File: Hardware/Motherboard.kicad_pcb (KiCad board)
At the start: 2 copper layers, 130 x 80 mm, 54 parts, among them J1 BME680, J2 JTAG, J3 Display_1, J4 Display_2, J5 Buttons, J6 USB, J7 MUSBD111M0_Supply, Q1 DMG3414U, SW1 Button_Plus, SW2 Button_Minus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

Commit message: [Hardware] Filled some empty bottom layer areas with ground plane.
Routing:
- net GND: vias 81 -> 94
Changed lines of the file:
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@@
     (thickness 1.6)
     (drawings 8)
-    (tracks 464)
+    (tracks 477)
     (zones 0)
     (modules 54)
@@
   (via (at 218.95 127.62) (size 0.8) (drill 0.4) (layers F.Cu B.Cu) (net 2))
   (via (at 218.95 130.62) (size 0.8) (drill 0.4) (layers F.Cu B.Cu) (net 2))
+  (via (at 150.162 73.66) (size 0.8) (drill 0.4) (layers F.Cu B.Cu) (net 2))
+  (via (at 150.162 76.708) (size 0.8) (drill 0.4) (layers F.Cu B.Cu) (net 2))
+  (via (at 168.958 111.76) (size 0.8) (drill 0.4) (layers F.Cu B.Cu) (net 2))
+  (via (at 177.086 119.38) (size 0.8) (drill 0.4) (layers F.Cu B.Cu) (net 2))
+  (via (at 180.388 121.412) (size 0.8) (drill 0.4) (layers F.Cu B.Cu) (net 2))
+  (via (at 182.928 121.412) (size 0.8) (drill 0.4) (layers F.Cu B.Cu) (net 2))
+  (via (at 185.468 121.412) (size 0.8) (drill 0.4) (layers F.Cu B.Cu) (net 2))
+  (via (at 188.008 121.412) (size 0.8) (drill 0.4) (layers F.Cu B.Cu) (net 2))
+  (via (at 190.548 121.412) (size 0.8) (drill 0.4) (layers F.Cu B.Cu) (net 2))
+  (via (at 193.088 121.412) (size 0.8) (drill 0.4) (layers F.Cu B.Cu) (net 2))
+  (via (at 195.628 121.666) (size 0.8) (drill 0.4) (layers F.Cu B.Cu) (net 2))
+  (via (at 170.482 87.63) (size 0.8) (drill 0.4) (layers F.Cu B.Cu) (net 2))
+  (via (at 174.038 87.63) (size 0.8) (drill 0.4) (layers F.Cu B.Cu) (net 2))
   (segment (start 168.91 83.82) (end 168.91 93.075) (width 0.5) (layer F.Cu) (net 3))
   (segment (start 171.26 95.425) (end 171.26 95.9) (width 0.5) (layer F.Cu) (net 3))

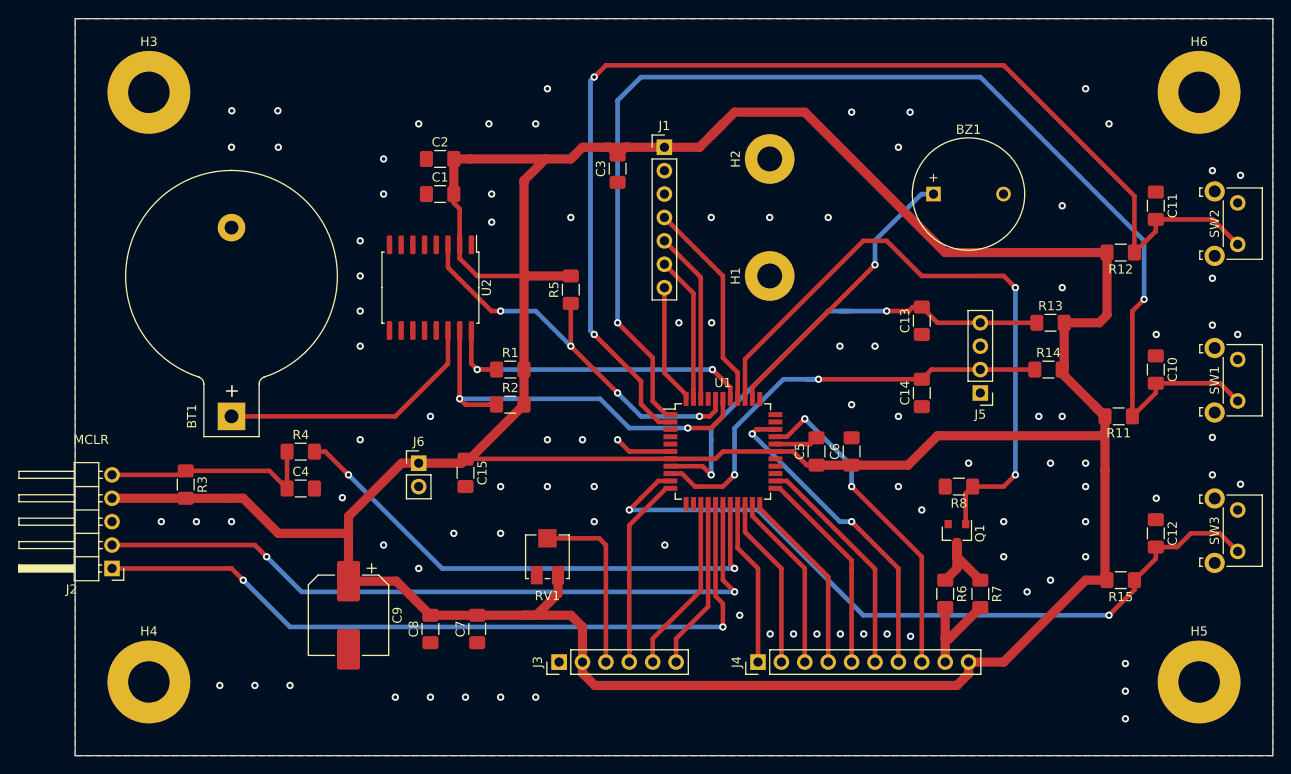
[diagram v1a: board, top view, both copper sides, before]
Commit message: [Hardware] Displayed connectors usage and button names on PCB.
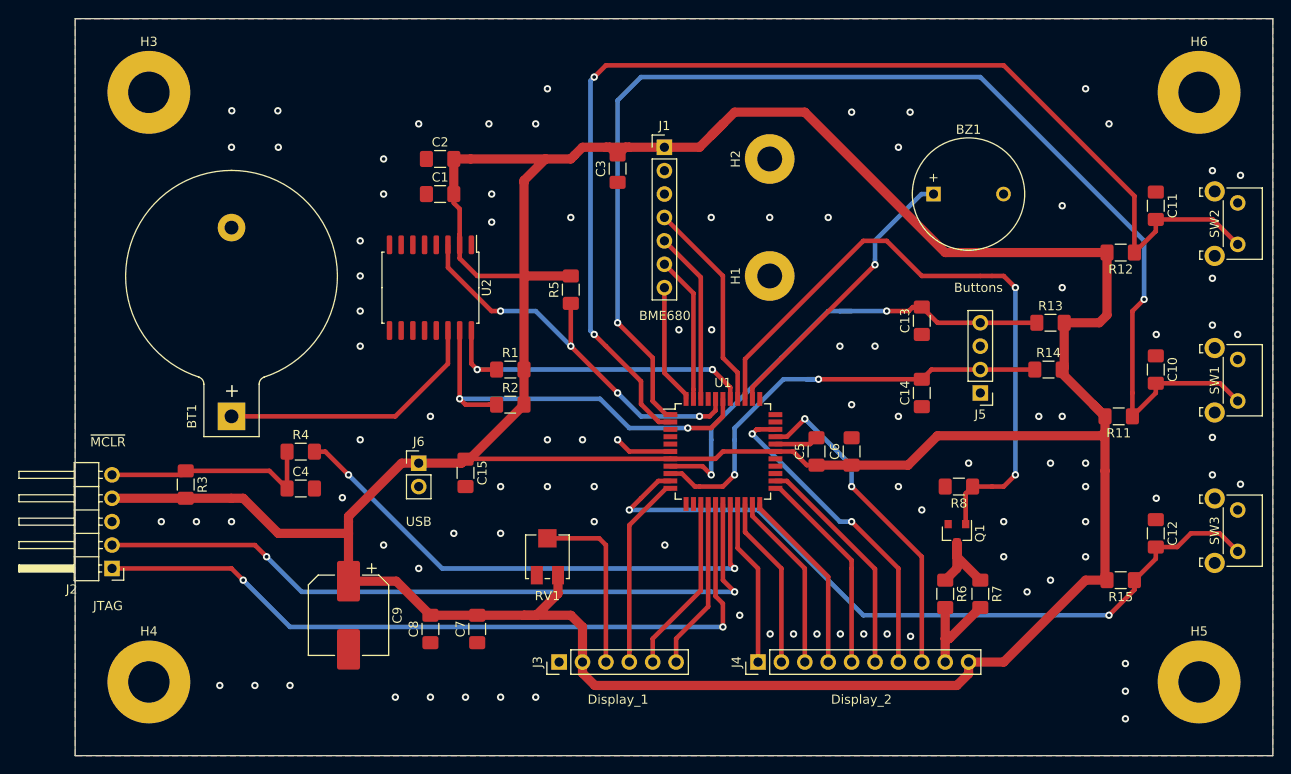
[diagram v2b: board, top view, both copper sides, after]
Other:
- board text added: "+"
- board text added: "-"
- board text added: "SET"
- board text added: "~MCLR~"
- board text removed: "MCLR"
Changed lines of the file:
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@@
   (general
     (thickness 1.6)
-    (drawings 8)
+    (drawings 11)
     (tracks 477)
     (zones 0)
@@
   )
   (setup
-    (last_trace_width 1)
+    (last_trace_width 0.5)
     (user_trace_width 0.5)
     (user_trace_width 1)
@@
       (effects (font (size 1 1) (thickness 0.15)))
     )
-    (fp_text value USB (at 0 4.87) (layer F.Fab)
+    (fp_text value USB (at 0 6.35) (layer F.SilkS)
       (effects (font (size 1 1) (thickness 0.15)))
     )
@@
       (effects (font (size 1 1) (thickness 0.15)))
     )
-    (fp_text value Buttons (at 0 9.95) (layer F.Fab)
+    (fp_text value Buttons (at 0.206 11.43) (layer F.SilkS)
       (effects (font (size 1 1) (thickness 0.15)))
     )
@@
       (effects (font (size 1 1) (thickness 0.15)))
     )
-    (fp_text value Display_2 (at 0 25.19 90) (layer F.Fab)
+    (fp_text value Display_2 (at -4.064 11.224 180) (layer F.SilkS)
       (effects (font (size 1 1) (thickness 0.15)))
     )
@@
       (effects (font (size 1 1) (thickness 0.15)))
     )
-    (fp_text value Display_1 (at 0 15.03 90) (layer F.Fab)
+    (fp_text value Display_1 (at -4.064 6.398 180) (layer F.SilkS)
       (effects (font (size 1 1) (thickness 0.15)))
     )
@@
       (effects (font (size 1 1) (thickness 0.15)))
     )
-    (fp_text value JTAG (at 4.385 12.43) (layer F.Fab)
+    (fp_text value JTAG (at 0.444 -4.064) (layer F.SilkS)
       (effects (font (size 1 1) (thickness 0.15)))
     )
@@
       (effects (font (size 1 1) (thickness 0.15)))
     )
-    (fp_text value BME680 (at 0 17.57) (layer F.Fab)
+    (fp_text value BME680 (at 0.048 18.288) (layer F.SilkS)
       (effects (font (size 1 1) (thickness 0.15)))
     )
@@
     )
   )
+  (gr_text SET (at 231.442 117.348) (layer F.Mask)
+    (effects (font (size 1.5 1.5) (thickness 0.3)))
+  )
+  (gr_text - (at 231.442 100.584) (layer F.Mask)
+    (effects (font (size 1.5 1.5) (thickness 0.3)))
+  )
+  (gr_text + (at 231.442 83.82) (layer F.Mask)
+    (effects (font (size 1.5 1.5) (thickness 0.3)))
+  )
   (dimension 80 (width 0.12) (layer F.SilkS)
     (gr_text "80,000 mm" (at 91.68 94.62 90) (layer F.SilkS)
@@
     (effects (font (size 1.5 1.5) (thickness 0.3)))
   )
-  (gr_text MCLR (at 106.68 100.33) (layer F.SilkS)
+  (gr_text ~MCLR~ (at 108.506 100.584) (layer F.SilkS)
     (effects (font (size 1 1) (thickness 0.15)))
   )
@@
   (via (at 193.088 121.412) (size 0.8) (drill 0.4) (layers F.Cu B.Cu) (net 2))
   (via (at 195.628 121.666) (size 0.8) (drill 0.4) (layers F.Cu B.Cu) (net 2))
-  (via (at 170.482 87.63) (size 0.8) (drill 0.4) (layers F.Cu B.Cu) (net 2))
-  (via (at 174.038 87.63) (size 0.8) (drill 0.4) (layers F.Cu B.Cu) (net 2))
+  (via (at 170.482 88.392) (size 0.8) (drill 0.4) (layers F.Cu B.Cu) (net 2))
+  (via (at 174.038 88.392) (size 0.8) (drill 0.4) (layers F.Cu B.Cu) (net 2))
   (segment (start 168.91 83.82) (end 168.91 93.075) (width 0.5) (layer F.Cu) (net 3))
   (segment (start 171.26 95.425) (end 171.26 95.9) (width 0.5) (layer F.Cu) (net 3))

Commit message: [Hardware] Replaced each supply part by a generic one to avoid creating a new symbol for every supply part.
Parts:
- J7: value MUSBD111M0_Supply -> USB_Connector_690-W05-260-044; footprint Empty_Footprint:Empty_Footprint -> Supply:Supply_Part
- SW4, SW5, U3: footprint Empty_Footprint:Empty_Footprint -> Supply:Supply_Part
- U4: value DEM20485SYH-LY_Supply -> LCD_DEM20485SYH-LY; footprint Empty_Footprint:Empty_Footprint -> Supply:Supply_Part
- moved SW5 44.5 mm to (71.9, 66.0)
- moved J7 37.9 mm to (59.2, 92.7)
- moved SW4 29.9 mm to (59.2, 65.9)
- moved U3 22.1 mm to (59.2, 74.9)
- moved U4 15.9 mm to (59.2, 83.8)
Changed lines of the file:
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@@
     (add_net "Net-(J4-Pad9)")
+  )
+  (module Supply:Supply_Part (layer F.Cu)
+    (at 59.23 83.82)
+    (attr virtual)
+    (fp_text reference U4 (at -3.175 3.81) (layer Eco1.User)
+      (effects (font (size 1 1) (thickness 0.15)))
+    )
+    (fp_text value LCD_DEM20485SYH-LY (at 0 -0.5) (layer F.Fab) hide
+      (effects (font (size 1 1) (thickness 0.15)))
+    )
+    (fp_line (start -5.08 2.54) (end -5.08 0) (layer Eco1.User) (width 0.12))
+    (fp_line (start 5.08 2.54) (end -5.08 2.54) (layer Eco1.User) (width 0.12))
+    (fp_line (start 5.08 -2.54) (end 5.08 2.54) (layer Eco1.User) (width 0.12))
+    (fp_line (start -5.08 -2.54) (end 5.08 -2.54) (layer Eco1.User) (width 0.12))
+    (fp_line (start -5.08 0) (end -5.08 -2.54) (layer Eco1.User) (width 0.12))
+  )
+  (module Supply:Supply_Part (layer F.Cu)
+    (at 59.23 74.93)
+    (attr virtual)
+    (fp_text reference U3 (at -3.175 3.81) (layer Eco1.User)
+      (effects (font (size 1 1) (thickness 0.15)))
+    )
+    (fp_text value Adafruit_BME680 (at 0 -0.5) (layer F.Fab) hide
+      (effects (font (size 1 1) (thickness 0.15)))
+    )
+    (fp_line (start -5.08 2.54) (end -5.08 0) (layer Eco1.User) (width 0.12))
+    (fp_line (start 5.08 2.54) (end -5.08 2.54) (layer Eco1.User) (width 0.12))
+    (fp_line (start 5.08 -2.54) (end 5.08 2.54) (layer Eco1.User) (width 0.12))
+    (fp_line (start -5.08 -2.54) (end 5.08 -2.54) (layer Eco1.User) (width 0.12))
+    (fp_line (start -5.08 0) (end -5.08 -2.54) (layer Eco1.User) (width 0.12))
+  )
+  (module Supply:Supply_Part (layer F.Cu)
+    (at 71.93 66.04)
+    (attr virtual)
+    (fp_text reference SW5 (at -3.175 3.81) (layer Eco1.User)
+      (effects (font (size 1 1) (thickness 0.15)))
+    )
+    (fp_text value Push_Button_R1500 (at 0 -0.5) (layer F.Fab) hide
+      (effects (font (size 1 1) (thickness 0.15)))
+    )
+    (fp_line (start -5.08 2.54) (end -5.08 0) (layer Eco1.User) (width 0.12))
+    (fp_line (start 5.08 2.54) (end -5.08 2.54) (layer Eco1.User) (width 0.12))
+    (fp_line (start 5.08 -2.54) (end 5.08 2.54) (layer Eco1.User) (width 0.12))
+    (fp_line (start -5.08 -2.54) (end 5.08 -2.54) (layer Eco1.User) (width 0.12))
+    (fp_line (start -5.08 0) (end -5.08 -2.54) (layer Eco1.User) (width 0.12))
+  )
+  (module Supply:Supply_Part (layer F.Cu)
+    (at 59.23 65.89)
+    (attr virtual)
+    (fp_text reference SW4 (at -3.175 3.81) (layer Eco1.User)
+      (effects (font (size 1 1) (thickness 0.15)))
+    )
+    (fp_text value Inverter_8013 (at 0 -0.5) (layer F.Fab) hide
+      (effects (font (size 1 1) (thickness 0.15)))
+    )
+    (fp_line (start -5.08 2.54) (end -5.08 0) (layer Eco1.User) (width 0.12))
+    (fp_line (start 5.08 2.54) (end -5.08 2.54) (layer Eco1.User) (width 0.12))
+    (fp_line (start 5.08 -2.54) (end 5.08 2.54) (layer Eco1.User) (width 0.12))
+    (fp_line (start -5.08 -2.54) (end 5.08 -2.54) (layer Eco1.User) (width 0.12))
+    (fp_line (start -5.08 0) (end -5.08 -2.54) (layer Eco1.User) (width 0.12))
+  )
+  (module Supply:Supply_Part (layer F.Cu)
+    (at 59.23 92.71)
+    (attr virtual)
+    (fp_text reference J7 (at -3.175 3.81) (layer Eco1.User)
+      (effects (font (size 1 1) (thickness 0.15)))
+    )
+    (fp_text value USB_Connector_690-W05-260-044 (at 0 -0.5) (layer F.Fab) hide
+      (effects (font (size 1 1) (thickness 0.15)))
+    )
+    (fp_line (start -5.08 2.54) (end -5.08 0) (layer Eco1.User) (width 0.12))
+    (fp_line (start 5.08 2.54) (end -5.08 2.54) (layer Eco1.User) (width 0.12))
+    (fp_line (start 5.08 -2.54) (end 5.08 2.54) (layer Eco1.User) (width 0.12))
+    (fp_line (start -5.08 -2.54) (end 5.08 -2.54) (layer Eco1.User) (width 0.12))
+    (fp_line (start -5.08 0) (end -5.08 -2.54) (layer Eco1.User) (width 0.12))
   )
   (module Button_Switch_THT:SW_Tactile_SKHH_Angled (layer F.Cu)
@@
     )
   )
-  (module Empty_Footprint:Empty_Footprint (layer F.Cu)
-    (at 72.39 128.27)
-    (fp_text reference J7 (at -3.81 6.35) (layer Eco1.User)
-      (effects (font (size 1 1) (thickness 0.15)))
-    )
-    (fp_text value MUSBD111M0_Supply (at 0 8.89) (layer Eco1.User)
-      (effects (font (size 1 1) (thickness 0.15)))
-    )
-    (fp_line (start 7.62 -3.81) (end -7.62 -3.81) (layer Eco1.User) (width 0.12))
-    (fp_line (start 7.62 5.08) (end 7.62 -3.81) (layer Eco1.User) (width 0.12))
-    (fp_line (start -7.62 5.08) (end 7.62 5.08) (layer Eco1.User) (width 0.12))
-    (fp_line (start -7.62 -3.81) (end -7.62 5.08) (layer Eco1.User) (width 0.12))
-  )
-  (module Empty_Footprint:Empty_Footprint (layer F.Cu)
-    (at 72.39 110.49)
-    (fp_text reference SW5 (at -3.81 6.35) (layer Eco1.User)
-      (effects (font (size 1 1) (thickness 0.15)))
-    )
-    (fp_text value Push_Button_R1500 (at 0 8.89) (layer Eco1.User)
-      (effects (font (size 1 1) (thickness 0.15)))
-    )
-    (fp_line (start 7.62 -3.81) (end -7.62 -3.81) (layer Eco1.User) (width 0.12))
-    (fp_line (start 7.62 5.08) (end 7.62 -3.81) (layer Eco1.User) (width 0.12))
-    (fp_line (start -7.62 5.08) (end 7.62 5.08) (layer Eco1.User) (width 0.12))
-    (fp_line (start -7.62 -3.81) (end -7.62 5.08) (layer Eco1.User) (width 0.12))
-  )
-  (module Empty_Footprint:Empty_Footprint (layer F.Cu)
-    (at 72.39 92.71)
-    (fp_text reference SW4 (at -3.81 6.35) (layer Eco1.User)
-      (effects (font (size 1 1) (thickness 0.15)))
-    )
-    (fp_text value Inverter_8013 (at 0 8.89) (layer Eco1.User)
-      (effects (font (size 1 1) (thickness 0.15)))
-    )
-    (fp_line (start 7.62 -3.81) (end -7.62 -3.81) (layer Eco1.User) (width 0.12))
-    (fp_line (start 7.62 5.08) (end 7.62 -3.81) (layer Eco1.User) (width 0.12))
-    (fp_line (start -7.62 5.08) (end 7.62 5.08) (layer Eco1.User) (width 0.12))
-    (fp_line (start -7.62 -3.81) (end -7.62 5.08) (layer Eco1.User) (width 0.12))
-  )
   (module Capacitor_SMD:C_1206_3216Metric_Pad1.42x1.75mm_HandSolder (layer F.Cu)
     (at 129.4375 105.62)
@@
     )
   )
-  (module Empty_Footprint:Empty_Footprint (layer F.Cu)
-    (at 72.39 74.93)
-    (fp_text reference U4 (at -3.81 6.35) (layer Eco1.User)
-      (effects (font (size 1 1) (thickness 0.15)))
-    )
-    (fp_text value DEM20485SYH-LY_Supply (at 0 8.89) (layer Eco1.User)
-      (effects (font (size 1 1) (thickness 0.15)))
-    )
-    (fp_line (start 7.62 -3.81) (end -7.62 -3.81) (layer Eco1.User) (width 0.12))
-    (fp_line (start 7.62 5.08) (end 7.62 -3.81) (layer Eco1.User) (width 0.12))
-    (fp_line (start -7.62 5.08) (end 7.62 5.08) (layer Eco1.User) (width 0.12))
-    (fp_line (start -7.62 -3.81) (end -7.62 5.08) (layer Eco1.User) (width 0.12))
-  )
-  (module Empty_Footprint:Empty_Footprint (layer F.Cu)
-    (at 72.39 57.15)
-    (fp_text reference U3 (at -3.81 6.35) (layer Eco1.User)
-      (effects (font (size 1 1) (thickness 0.15)))
-    )
-    (fp_text value Adafruit_BME680 (at 0 8.89) (layer Eco1.User)
-      (effects (font (size 1 1) (thickness 0.15)))
-    )
-    (fp_line (start 7.62 -3.81) (end -7.62 -3.81) (layer Eco1.User) (width 0.12))
-    (fp_line (start 7.62 5.08) (end 7.62 -3.81) (layer Eco1.User) (width 0.12))
-    (fp_line (start -7.62 5.08) (end 7.62 5.08) (layer Eco1.User) (width 0.12))
-    (fp_line (start -7.62 -3.81) (end -7.62 5.08) (layer Eco1.User) (width 0.12))
-  )
   (module MountingHole:MountingHole_4.5mm_Pad (layer F.Cu)

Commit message: [Hardware] Swapped 'plus' and 'minus' buttons in both schematic and PCB to match final buttons position.
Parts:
- SW1: value Button_Plus -> Button_Minus
- SW2: value Button_Minus -> Button_Plus
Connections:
- C10 pad 2: /PLUS_BUTTON -> /MINUS_BUTTON
- C11 pad 2: /MINUS_BUTTON -> /PLUS_BUTTON
- R11 pad 1: /PLUS_BUTTON -> /MINUS_BUTTON
- R12 pad 1: /MINUS_BUTTON -> /PLUS_BUTTON
- SW1 pad 2: /PLUS_BUTTON -> /MINUS_BUTTON
- SW2 pad 2: /MINUS_BUTTON -> /PLUS_BUTTON
- U1 pad 1: /PLUS_BUTTON -> /MINUS_BUTTON
- U1 pad 2: /MINUS_BUTTON -> /PLUS_BUTTON
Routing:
- net /PLUS_BUTTON: track 136.2 -> 127.7 mm
- net /MINUS_BUTTON: track 127.7 -> 136.2 mm
